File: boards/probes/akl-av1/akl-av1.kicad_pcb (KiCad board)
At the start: 4 copper layers, 23.8 x 10.5 mm, 35 parts, among them J1 U.FL, J2 TIPRES, J3 TIPRES, J4 SMPM, U1 LTC1983-5, U2 ADP7142ACPZN-R7, U3 ADP7182_DFN8, U4 BUF802

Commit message: Finished v0.1 AKL-AV1 for fab
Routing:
- added copper zone on B.Cu, net /Power Supply/6V0
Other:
- board text added: "AKL-AV1 v0.1 2022-05-27 A. Zonenberg"
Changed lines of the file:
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@@
       (outputformat 1)
       (mirror false)
-      (drillshape 1)
+      (drillshape 0)
       (scaleselection 1)
-      (outputdirectory "")
+      (outputdirectory "output/")
     )
   )
@@
   (gr_line (start 51.5 49.25) (end 51.5 52.75) (layer "Edge.Cuts") (width 0.1))
   (gr_line (start 71 54.25) (end 47.25 54.25) (layer "Edge.Cuts") (width 0.1))
+  (gr_text "AKL-AV1\nv0.1\n2022-05-27\nA. Zonenberg" (at 58.3 46.2) (layer "B.SilkS")
+    (effects (font (size 0.75 0.75) (thickness 0.1)) (justify mirror))
+  )
   (segment (start 50.6 47.65) (end 51.424502 47.65) (width 0.25) (layer "F.Cu") (net 1))
   (segment (start 52.55 47.65) (end 52.5 47.6) (width 0.25) (layer "F.Cu") (net 1))
@@
       )
     )
+  )
+  (zone (net 1) (net_name "/Power Supply/6V0") (layer "B.Cu") (hatch edge 0.508)
+    (connect_pads (clearance 0.15))
+    (min_thickness 0.15) (filled_areas_thickness no)
+    (fill yes (thermal_gap 0.5) (thermal_bridge_width 0.5))
+    (polygon
+      (pts
+        (xy 57 47.25)
+        (xy 62.75 47.25)
+        (xy 63.25 46.75)
+        (xy 63.25 46.5)
+        (xy 65 46.5)
+        (xy 65 44.25)
+        (xy 67 44.25)
+        (xy 67 46.5)
+        (xy 66.5 46.5)
+        (xy 66.5 48.5)
+        (xy 59.5 48.5)
+        (xy 59.5 51.25)
+        (xy 58 51.25)
+        (xy 58 48)
+        (xy 54.5 48)
+        (xy 54.5 45)
+        (xy 53 45)
+        (xy 53 48)
+        (xy 51.5 48)
+        (xy 51.5 44)
+        (xy 57 44)
+      )
+    )

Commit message: Cleanup to ground plane under tip
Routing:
- net /GND: track 83.2 -> 82.3 mm
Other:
- board text added: "AKL-AV1 v0.1b 2022-05-27 A. Zonenberg"
- board text removed: "AKL-AV1 v0.1 2022-05-27 A. Zonenberg"
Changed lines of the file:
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@@
   (gr_line (start 51.5 49.25) (end 51.5 52.75) (layer "Edge.Cuts") (width 0.1))
   (gr_line (start 71 54.25) (end 47.25 54.25) (layer "Edge.Cuts") (width 0.1))
-  (gr_text "AKL-AV1\nv0.1\n2022-05-27\nA. Zonenberg" (at 58.3 46.2) (layer "B.SilkS")
+  (gr_text "AKL-AV1\nv0.1b\n2022-05-27\nA. Zonenberg" (at 58.3 46.2) (layer "B.SilkS")
     (effects (font (size 0.75 0.75) (thickness 0.1)) (justify mirror))
   )
@@
   (segment (start 65.8 52.7) (end 65.25 53.25) (width 0.25) (layer "In1.Cu") (net 2))
   (segment (start 62 51) (end 62.5 51) (width 0.25) (layer "In1.Cu") (net 2))
+  (segment (start 66.9 46.5) (end 65.1 48.3) (width 0.25) (layer "In1.Cu") (net 2))
   (segment (start 50 46.4) (end 49 46.4) (width 0.25) (layer "In1.Cu") (net 2))
   (segment (start 51.25 48.75) (end 50.25 48.75) (width 0.25) (layer "In1.Cu") (net 2))
@@
   (segment (start 52.25 49.5) (end 52.25 48.75) (width 0.25) (layer "In1.Cu") (net 2))
   (segment (start 60.5 53.25) (end 59 53.25) (width 0.25) (layer "In1.Cu") (net 2))
-  (segment (start 69.8 48.2) (end 70 48) (width 0.25) (layer "In1.Cu") (net 2))
   (segment (start 49 46.4) (end 48.7 46.1) (width 0.25) (layer "In1.Cu") (net 2))
   (segment (start 55.25 49.5) (end 55.25 52.5) (width 0.25) (layer "In1.Cu") (net 2))
@@
   (segment (start 58.75 52.35) (end 58.7 52.4) (width 0.25) (layer "In1.Cu") (net 2))
   (segment (start 63.9 48.3) (end 62.5 49.7) (width 0.25) (layer "In1.Cu") (net 2))
+  (segment (start 68.5 46.5) (end 66.9 46.5) (width 0.25) (layer "In1.Cu") (net 2))
   (segment (start 62.5 51) (end 62.5 51.75) (width 0.25) (layer "In1.Cu") (net 2))
-  (segment (start 69.8 53) (end 69.8 48.2) (width 0.25) (layer "In1.Cu") (net 2))
   (segment (start 69.25 46.5) (end 68.5 46.5) (width 0.25) (layer "In1.Cu") (net 2))
   (segment (start 58.35 52.4) (end 58 52.75) (width 0.25) (layer "In1.Cu") (net 2))

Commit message: Rev 0.2 of AKL-AV1
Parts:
- removed R12: 49.9, azonenberg_pcb:EIA_0402_RES_NOSILK
- removed R9: 0, azonenberg_pcb:EIA_0402_RES_NOSILK
- added C16: 800 fF, azonenberg_pcb:EIA_0402_CAP_NOSILK, B.Cu at (67.3, 50.3)
- added L1: FERRITE, azonenberg_pcb:EIA_0402_CAP_NOSILK, F.Cu at (55.5, 46.6)
- R7: value DNP -> 1M; footprint azonenberg_pcb:EIA_0402_RES_NOSILK -> azonenberg_pcb:EIA_0402_CAP_NOSILK
- moved R7 1.22 mm to (66.1, 49.8), turned to 90 degrees
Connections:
- C7 pad 1: /Power Supply/5V0_N -> Net-(C7-Pad1)
- R11 pad 2: /VAUX -> Net-(R11-Pad2)
- R7 pad 1: Net-(R7-Pad1) -> /VIN
- R7 pad 2: /VIN -> Net-(R11-Pad2)
- U1 pad 2: /Power Supply/5V0_N -> Net-(C7-Pad1)
- U4 pad 3: Net-(R7-Pad1) -> unconnected-(U4-Pad3)
- U4 pad 4: /VAUX -> unconnected-(U4-Pad4)
- U4 pad 6: Net-(R9-Pad2) -> unconnected-(U4-Pad6)
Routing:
- net /VAUX: track 4.36 -> 0.00 mm
- net /Power Supply/5V0_N: track 13.7 -> 10.2 mm, vias 7 -> 6
- net Net-(C7-Pad1): track 0.00 -> 2.44 mm, vias 0 -> 1
- net Net-(R11-Pad2): track 0.00 -> 1.89 mm, vias 0 -> 1
- net Net-(R9-Pad2): track 1.03 -> 0.00 mm
- net /VIN: track 4.35 -> 5.28 mm
- net Net-(R7-Pad1): track 0.85 -> 0.00 mm, vias 1 -> 0
- net /VOUT: track 4.14 -> 3.39 mm
- net /TIP: track 2.70 -> 3.41 mm
- net /4V5_N: track 26.2 -> 25.7 mm
- net /GND: track 82.3 -> 81.8 mm
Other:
- board text added: "AKL-AV1 v0.2 2022-06-21 A. Zonenberg"
- board text removed: "AKL-AV1 v0.1b 2022-05-27 A. Zonenberg"

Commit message: Updated AKL-AV1 design files for v0.3 prototype
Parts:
- added C17: 0.47 uF, azonenberg_pcb:EIA_0402_CAP_NOSILK, F.Cu at (64.4, 48.0)
- added C18: 56 pF, azonenberg_pcb:EIA_0402_CAP_NOSILK, B.Cu at (67.0, 50.0)
- added C19: 330 pF, azonenberg_pcb:EIA_0402_CAP_NOSILK, B.Cu at (63.8, 51.5)
- added C20: 100 pF, azonenberg_pcb:EIA_0402_CAP_NOSILK, B.Cu at (63.8, 49.0)
- added R12: 80.6K, azonenberg_pcb:EIA_0402_RES_NOSILK, B.Cu at (58.1, 51.5)
- added R13: 2K, azonenberg_pcb:EIA_0402_RES_NOSILK, F.Cu at (65.2, 49.5)
- added R14: 10M, azonenberg_pcb:EIA_0402_RES_NOSILK, F.Cu at (63.8, 50.9)
- added R9: 3312J-1-203E, azonenberg_pcb:RES_TRIM_BOURNS_3312, F.Cu at (67.8, 46.8)
- added U5: ADA4075-2, azonenberg_pcb:DFN_8_0.5MM_2x2MM_NOPAD, B.Cu at (65.8, 48.0)
- C16: value 800 fF -> 0.47 uF
- R11: value 3312J-1-103E1 -> 30; footprint azonenberg_pcb:RES_TRIM_BOURNS_3312 -> azonenberg_pcb:EIA_0402_RES_NOSILK; moved to B.Cu
- R6: value 1M -> 806K
- R7: value 1M -> 200K; footprint azonenberg_pcb:EIA_0402_CAP_NOSILK -> azonenberg_pcb:EIA_0402_RES_NOSILK; moved to F.Cu
- moved U2 5.78 mm to (63.5, 45.3), turned to 90 degrees
- moved R11 5.55 mm to (64.5, 51.5), turned to -90 degrees
- moved C3 4.98 mm to (63.1, 46.6), turned to 180 degrees
- moved C6 4.71 mm to (65.7, 45.4), turned to -90 degrees
- moved R4 4.60 mm to (66.7, 45.1)
- moved C16 3.93 mm to (67.8, 46.4), turned to 0 degrees
- moved R3 3.70 mm to (65.5, 45.6), turned to 90 degrees
- moved R1 2.25 mm to (60.5, 46.0)
- moved R7 2.20 mm to (65.2, 47.8)
- moved C4 2.00 mm to (61.0, 45.5)
- moved C2 1.75 mm to (55.6, 45.9)
- moved R2 1.75 mm to (60.0, 44.8)
- moved U3 1.75 mm to (58.2, 45.8)
- moved R8 1.61 mm to (61.8, 48.1)
- moved R6 1.57 mm to (65.6, 50.4), turned to 90 degrees
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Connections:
- C16 pad 1: /TIP -> /4V5_P
- C16 pad 2: /VIN -> /GND
- L1 pad 1: Net-(C7-Pad1) -> /Power Supply/5V0_N
- L1 pad 2: /Power Supply/5V0_N -> Net-(C7-Pad1)
- R11 pad 1: /4V5_P -> /VIN
- R11 pad 2: Net-(R11-Pad2) -> Net-(C19-Pad1)
- R6 pad 2: /GND -> Net-(R6-Pad2)
- R7 pad 1: /VIN -> Net-(R6-Pad2)
- R7 pad 2: Net-(R11-Pad2) -> /GND
- U4 pad 2: /VIN -> Net-(U4-Pad2)
- U4 pad 3: unconnected-(U4-Pad3) -> Net-(U4-Pad3)
- U4 pad 4: unconnected-(U4-Pad4) -> /VAUX
- U4 pad 6: unconnected-(U4-Pad6) -> /4V5_N
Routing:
- net Net-(R9-Pad1): track 0.00 -> 12.9 mm, vias 0 -> 1
- net /Power Supply/6V0: track 35.7 -> 29.0 mm
- net Net-(R13-Pad1): track 0.00 -> 2.95 mm, vias 0 -> 1
- net /GND: track 81.8 -> 84.4 mm, vias 48 -> 51
- net /4V5_N: track 25.7 -> 28.2 mm
- net /VAUX: track 0.00 -> 2.13 mm, vias 0 -> 1
- net Net-(R11-Pad2): track 1.89 -> 0.00 mm, vias 1 -> 0
- net Net-(R6-Pad2): track 0.00 -> 1.71 mm, vias 0 -> 1
- net /VIN: track 5.28 -> 3.58 mm
- net Net-(U4-Pad2): track 0.00 -> 1.70 mm, vias 0 -> 1
- net /TIP: track 3.41 -> 1.90 mm
- net Net-(U4-Pad3): track 0.00 -> 1.15 mm
- net /RBIAS: track 2.36 -> 1.27 mm
- net Net-(R12-Pad2): track 2.25 -> 1.17 mm, vias 0 -> 1
- net Net-(C19-Pad1): track 0.00 -> 0.80 mm
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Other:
- board size 23.8 x 10.5 mm -> 22.9 x 10.5 mm
- board text added: "2022-07-03 A. Zonenberg"
- board text added: "AKL-AV1 v0.3"
- board text removed: "AKL-AV1 v0.2 2022-06-21 A. Zonenberg"

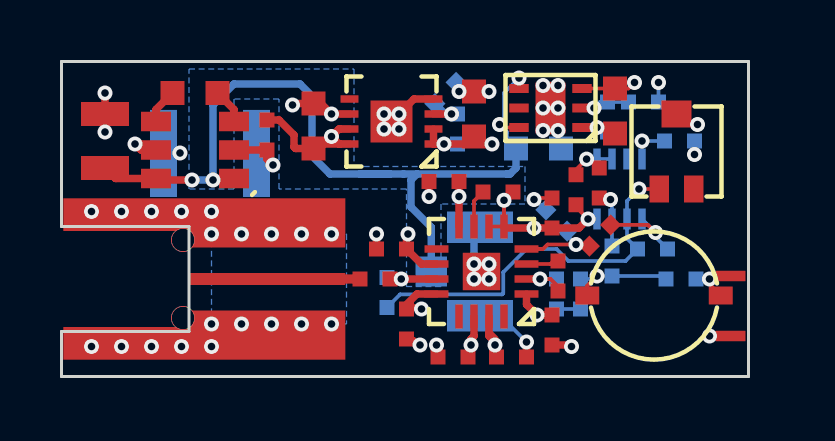
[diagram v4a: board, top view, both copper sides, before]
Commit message: Updated AKL-AV1 with v0.4 layout including OPA210 and noise filter
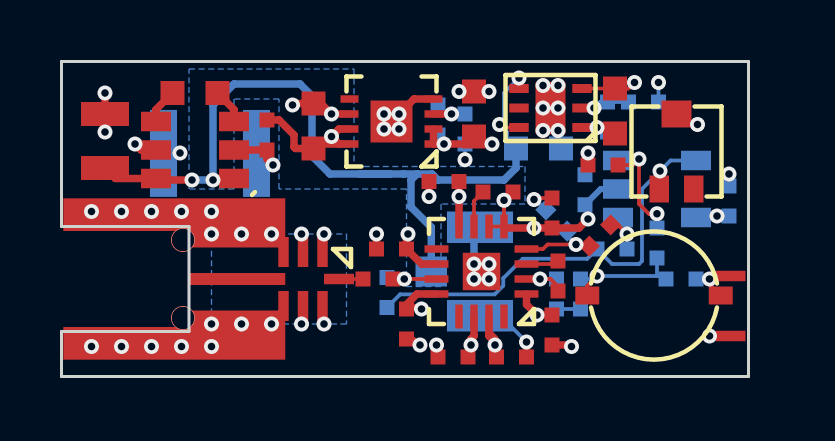
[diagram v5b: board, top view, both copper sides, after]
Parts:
- added FL1: LFCG-1800+, azonenberg_pcb:FILTER_MINICIRCUITS_LFCG, F.Cu at (55.3, 51.0)
- C17: moved to B.Cu
- C18: value 56 pF -> 75 pF
- J4: footprint azonenberg_pcb:CONN_SMPM_AMPHENOL_925-169J-51PT -> azonenberg_pcb:CONN_SMPM_AMPHENOL_925-169J-51PT_SHORT
- U5: value ADA4075-2 -> OPA210_SOT23_TI_DBV; footprint azonenberg_pcb:DFN_8_0.5MM_2x2MM_NOPAD -> azonenberg_pcb:SOT23_5
- moved C16 2.59 mm to (69.5, 48.4), turned to 90 degrees
- moved R6 1.62 mm to (67.1, 49.8)
- moved R2 1.36 mm to (60.7, 46.0), turned to -90 degrees
- moved C18 1.35 mm to (65.6, 50.0)
- moved U5 1.25 mm to (67.1, 48.0)
- moved R1 0.72 mm to (59.8, 45.7)
- moved R7 0.61 mm to (65.3, 47.2), turned to 180 degrees
- moved C17 0.30 mm to (64.7, 48.0)
- moved R10 0.10 mm to (57.8, 51.0)
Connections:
- C18 pad 1: Net-(R9-Pad1) -> Net-(C18-Pad1)
- J4 pad 1: /VOUT -> /FOUT
- R12 pad 1: Net-(R9-Pad1) -> Net-(C18-Pad1)
- R9 pad 1: Net-(R9-Pad1) -> Net-(C18-Pad1)
- U5 pad 2: Net-(R9-Pad1) -> /4V5_N
- U5 pad 4: /4V5_N -> Net-(C18-Pad1)
- U5 pad 5: /GND -> /4V5_P
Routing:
- net Net-(C18-Pad1): track 0.00 -> 14.9 mm, vias 0 -> 1
- net Net-(R9-Pad1): track 12.9 -> 0.00 mm, vias 1 -> 0
- net /GND: track 84.4 -> 90.0 mm, vias 51 -> 52
- net /4V5_P: track 24.2 -> 28.2 mm
- net Net-(R6-Pad2): track 1.71 -> 4.14 mm, vias 1 -> 2
- net /VOUT: track 3.10 -> 0.80 mm
- net Net-(R13-Pad1): track 2.95 -> 1.60 mm
- net Net-(R10-Pad1): track 1.17 -> 2.05 mm
- net Net-(R1-Pad2): track 1.30 -> 0.60 mm
- net /VIN: track 3.58 -> 4.18 mm
- net /4V5_N: track 28.2 -> 27.6 mm
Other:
- board text added: "2022-07-16 A. Zonenberg"
- board text added: "AKL-AV1 v0.4"
- board text removed: "2022-07-03 A. Zonenberg"
- board text removed: "AKL-AV1 v0.3"

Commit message: AKL-AV1 v0.5 with new power supply, GSG tip, clearance fixes, and passive CTLE
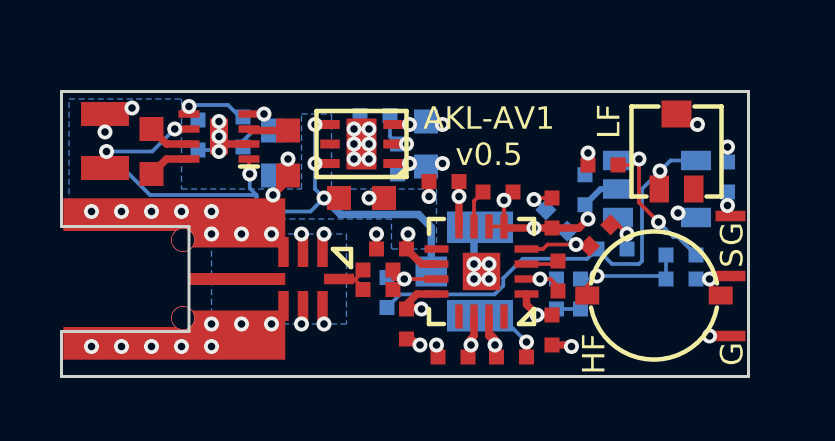
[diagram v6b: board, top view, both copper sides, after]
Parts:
- removed C7: 22 uF, azonenberg_pcb:EIA_1210_CAP_NOSILK
- removed L1: FERRITE, azonenberg_pcb:EIA_0402_CAP_NOSILK
- removed U3: ADP7182_DFN8, azonenberg_pcb:DFN_8_0.5MM_3x3MM
- added C21: 2 pF, azonenberg_pcb:EIA_0402_CAP_NOSILK, F.Cu at (57.8, 51.4)
- added J5: TIPRES, azonenberg_pcb:EDGELAUNCH_350UM, F.Cu at (69.5, 48.9)
- C3: moved to F.Cu
- C4: value 4.7 uF -> 1 uF
- C5: value 1 uF -> 4.7 uF; moved to B.Cu
- C6: moved to B.Cu
- R1: value 88.7K -> 255K
- R2: value 33K 1% -> 95.3K
- U1: value LTC1983-5 -> LM27761; footprint azonenberg_pcb:SOT23_6 -> azonenberg_pcb:DFN_8_0.5MM_2x2MM
- moved C4 10.8 mm to (50.2, 46.8)
- moved R4 8.96 mm to (57.7, 45.5), turned to 180 degrees
- moved R2 8.90 mm to (51.8, 46.2)
- moved R3 7.14 mm to (58.5, 47.0)
- moved R1 6.51 mm to (53.3, 46.1)
- moved U2 6.41 mm to (57.2, 46.5)
- moved C6 6.40 mm to (59.4, 46.5)
- moved C3 6.13 mm to (57.2, 48.3)
- moved C5 3.28 mm to (54.3, 46.8), turned to -90 degrees
- moved C2 1.24 mm to (54.8, 46.8)
- moved U1 0.92 mm to (52.5, 46.2), turned to 180 degrees
- moved R6 0.89 mm to (67.9, 50.2), turned to 0 degrees
- moved C16 0.80 mm to (69.5, 47.6), turned to -90 degrees
- moved R10 0.30 mm to (57.8, 50.7)
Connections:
- net /Power Supply/6V0 renamed /Power Supply/5V5
- C2 pad 1: /Power Supply/5V0_N -> /GND
- C2 pad 2: /GND -> Net-(C2-Pad2)
- C4 pad 1: /GND -> Net-(C4-Pad1)
- C4 pad 2: /4V5_N -> Net-(C4-Pad2)
- C5 pad 1: Net-(C5-Pad1) -> /4V5_N
- C5 pad 2: Net-(C5-Pad2) -> /GND
- R1 pad 2: Net-(R1-Pad2) -> /Power Supply/4V5_N_FB
- R2 pad 1: Net-(R1-Pad2) -> /Power Supply/4V5_N_FB
- U1 pad 2: Net-(C7-Pad1) -> /GND
- U1 pad 3: Net-(C5-Pad1) -> Net-(C2-Pad2)
- U1 pad 4: Net-(C5-Pad2) -> /4V5_N
- U1 pad 5: /GND -> /Power Supply/4V5_N_FB
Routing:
- net /Power Supply/5V0_N: track 10.1 -> 0.00 mm, vias 5 -> 0
- net /Power Supply/5V5: track 29.2 -> 23.1 mm, vias 4 -> 6
- net /4V5_P: track 28.2 -> 34.0 mm, vias 5 -> 7
- net /GND: track 90.0 -> 84.9 mm, vias 52 -> 51
- net /4V5_N: track 27.6 -> 31.6 mm, vias 8 -> 7
- net /Power Supply/4V5_N_FB: track 0.00 -> 2.66 mm, vias 0 -> 1
- net Net-(C7-Pad1): track 2.39 -> 0.00 mm, vias 1 -> 0
- net Net-(C4-Pad2): track 0.00 -> 1.46 mm
- net Net-(C4-Pad1): track 0.00 -> 1.46 mm
- net Net-(R6-Pad2): track 4.14 -> 5.51 mm
- net Net-(C2-Pad2): track 0.00 -> 1.32 mm
- net Net-(C5-Pad2): track 1.18 -> 0.00 mm
- net Net-(C5-Pad1): track 1.18 -> 0.00 mm
- net Net-(R1-Pad2): track 0.60 -> 0.00 mm, vias 1 -> 0
- net /VOUT: track 0.80 -> 1.33 mm
- removed copper zone on In2.Cu, net /Power Supply/5V0_N
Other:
- board size 22.9 x 10.5 mm -> 22.9 x 9.5 mm
- board text added: "2022 08-08"
- board text added: "5.5V"
- board text added: "A. Zonenberg"
- board text added: "AKL-AV1 v0.5"
- board text added: "G"
- board text added: "HF"
- board text added: "LF"
- board text added: "S"
- board text removed: "2022-07-16 A. Zonenberg"
- board text removed: "AKL-AV1 v0.4"

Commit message: Updated AKL-AV1 to v0.6
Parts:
- removed FL1: LFCG-1800+, azonenberg_pcb:FILTER_MINICIRCUITS_LFCG
- added C22: GJM1555C1H4R0WB01D, azonenberg_pcb:EIA_0402_CAP_NOSILK, F.Cu at (53.5, 51.5)
- added C7: GJM1555C1H1R1WB01D, azonenberg_pcb:EIA_0402_CAP_NOSILK, F.Cu at (55.2, 52.1)
- added L1: LQG15HN1N0S02D, azonenberg_pcb:EIA_0402_CAP_NOSILK, F.Cu at (56.2, 51.0)
- added L2: LQG15HN4N7C02D, azonenberg_pcb:EIA_0402_CAP_NOSILK, F.Cu at (54.7, 51.0)
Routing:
- net /GND: track 84.9 -> 82.9 mm, vias 51 -> 48
- net /FOUT: track 0.00 -> 1.57 mm
- net Net-(C7-Pad2): track 0.00 -> 1.13 mm
- net /VOUT: track 1.33 -> 0.78 mm
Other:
- board text added: "2022 10-06"
- board text added: "AKL-AV1 v0.6"
- board text removed: "2022 08-08"
- board text removed: "AKL-AV1 v0.5"
